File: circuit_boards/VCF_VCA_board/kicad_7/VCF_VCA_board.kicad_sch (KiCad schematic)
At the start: 7 parts, among them J2 MOD_BOARD_CON, J3 VCF_EXT_CON, SW1 SR1712F-0204

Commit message: Progress on circuit boards
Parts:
- added D101, D102: MMSZ5225B-7-F, Diode_SMD:D_SOD-123, symbol Device:D_Zener
- added R103: 1k, Resistor_SMD:R_0603_1608Metric, symbol Device:R
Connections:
- net GND: now also D102.1 (K)
- net VCF: now also R103.1
- new net: D101.2 (A), D102.2 (A)
- new net envelope_VCA/SIGNAL_IN: D101.1 (K), R103.2
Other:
- note removed: "TODO check the pole-mixing scheme, does the dry signal include the feedback or not?"
- moved on the sheet: C101, J2, J3, R101, R102, SW1A

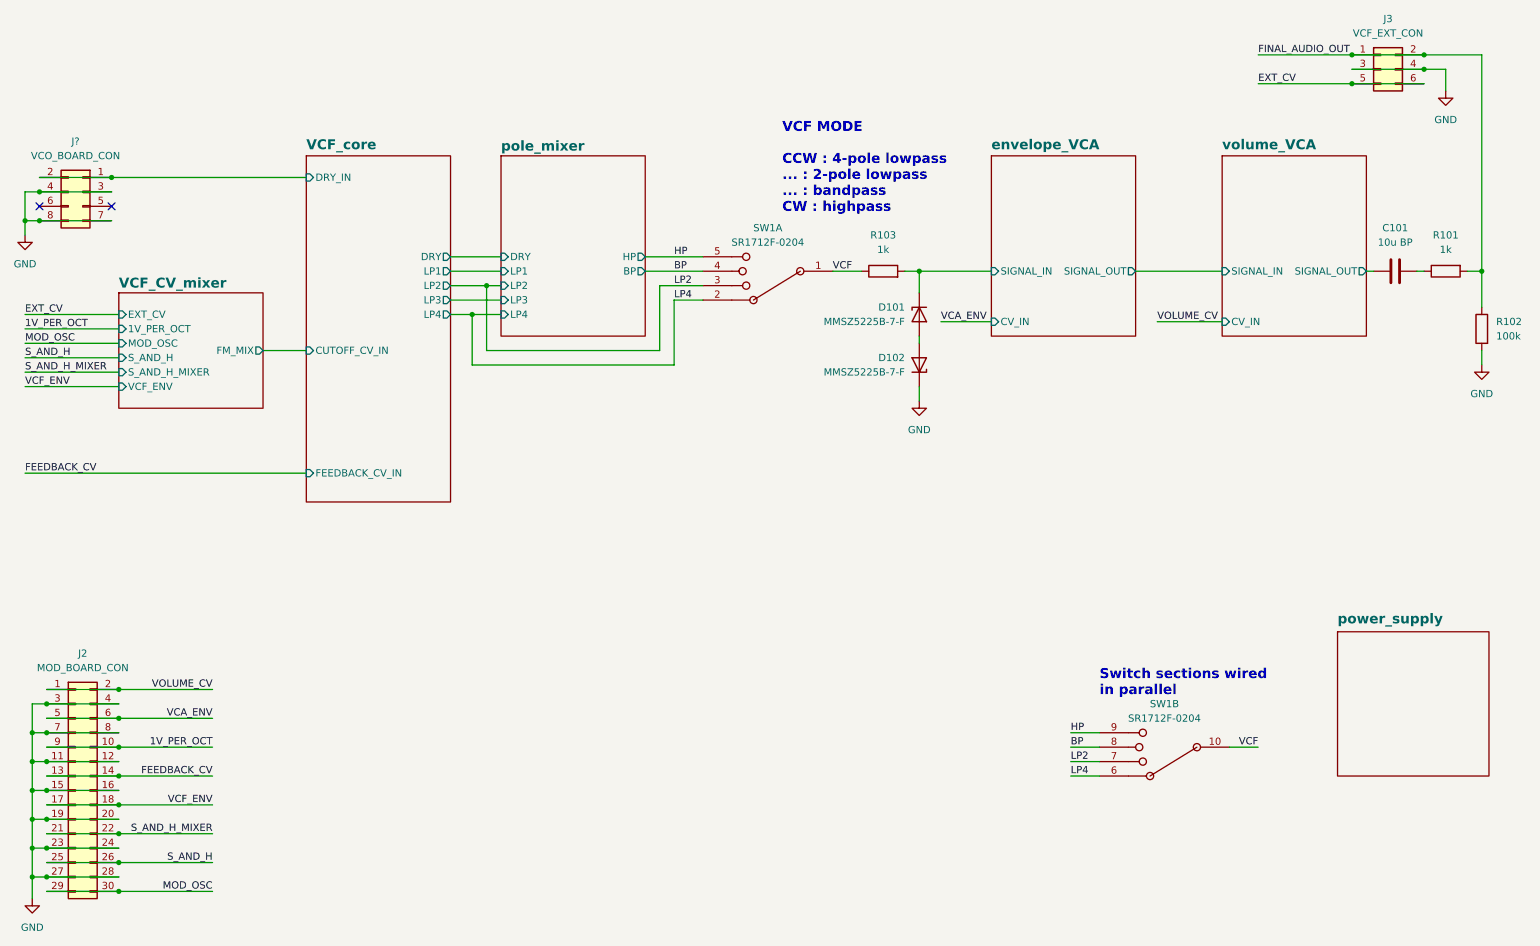
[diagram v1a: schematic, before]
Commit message: Update PCBs, tweak vals, add VCF CV from DAC
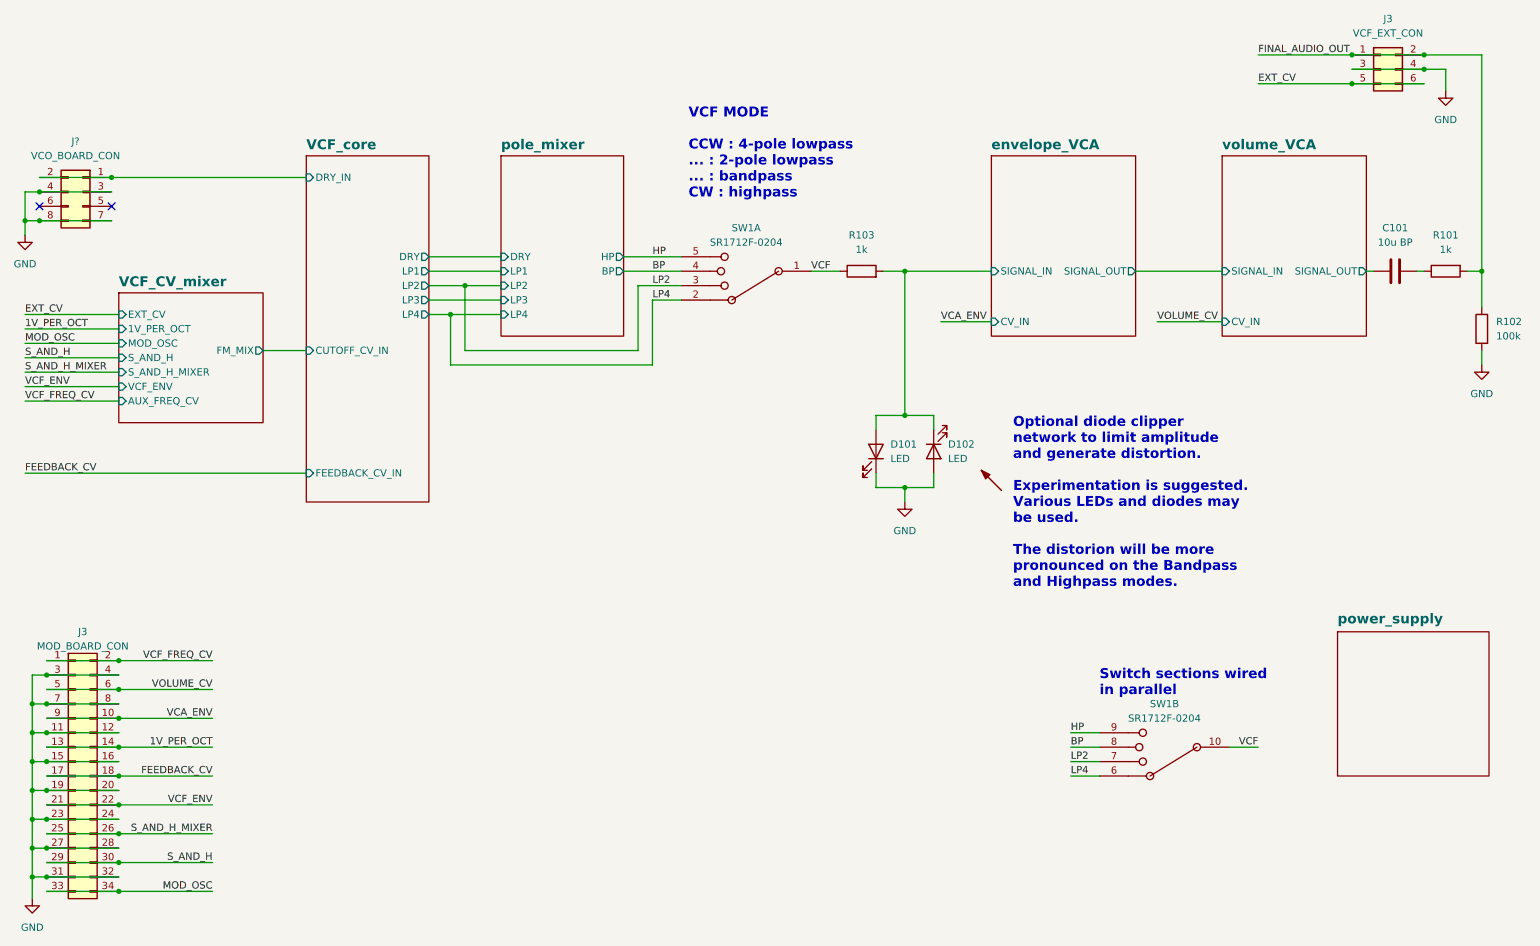
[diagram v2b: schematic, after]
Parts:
- removed D101, D102: MMSZ5225B-7-F, Diode_SMD:D_SOD-123, symbol Device:D_Zener
- removed J2: MOD_BOARD_CON, custom_footprints:30_pin_IDC-Header, symbol Connector_Generic:Conn_02x15_Odd_Even
- added D101, D102: LED, LED_THT:LED_D5.0mm, symbol Device:LED
- added J3: MOD_BOARD_CON, custom_footprints:34_pin_IDC_header, symbol Connector_Generic:Conn_02x17_Odd_Even
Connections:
- net 1V_PER_OCT: now also J3.13 (Pin_13), J3.14 (Pin_14)
- net FEEDBACK_CV: now also J3.17 (Pin_17), J3.18 (Pin_18)
- net GND: now also D101.1 (K), D102.2 (A), J3.11 (Pin_11), J3.12 (Pin_12), J3.15 (Pin_15), J3.16 (Pin_16), J3.19 (Pin_19), J3.20 (Pin_20), J3.23 (Pin_23), J3.24 (Pin_24), J3.27 (Pin_27), J3.28 (Pin_28), J3.3 (Pin_3), J3.31 (Pin_31), J3.32 (Pin_32), J3.4 (Pin_4), J3.7 (Pin_7), J3.8 (Pin_8)
- net MOD_OSC: now also J3.33 (Pin_33), J3.34 (Pin_34)
- net S_AND_H: now also J3.29 (Pin_29), J3.30 (Pin_30)
- net S_AND_H_MIXER: now also J3.25 (Pin_25), J3.26 (Pin_26)
- net VCA_ENV: now also J3.10 (Pin_10), J3.9 (Pin_9)
- net VCF_ENV: now also J3.21 (Pin_21), J3.22 (Pin_22)
- net VOLUME_CV: now also J3.5 (Pin_5), J3.6 (Pin_6)
- net envelope_VCA/SIGNAL_IN: now also D101.2 (A), D102.1 (K)
- new net VCF_FREQ_CV: J3.1 (Pin_1), J3.2 (Pin_2)
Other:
- sheet VCF_CV_mixer ports: added AUX_FREQ_CV; removed none
- note added: "Optional diode clipper network to limit amplitude and generate distortion. Experimentation is suggested. Various LEDs and diodes may be used. The distorion will be more pronounced on the Bandpass and Highpass modes."
- moved on the sheet: R103, SW1A

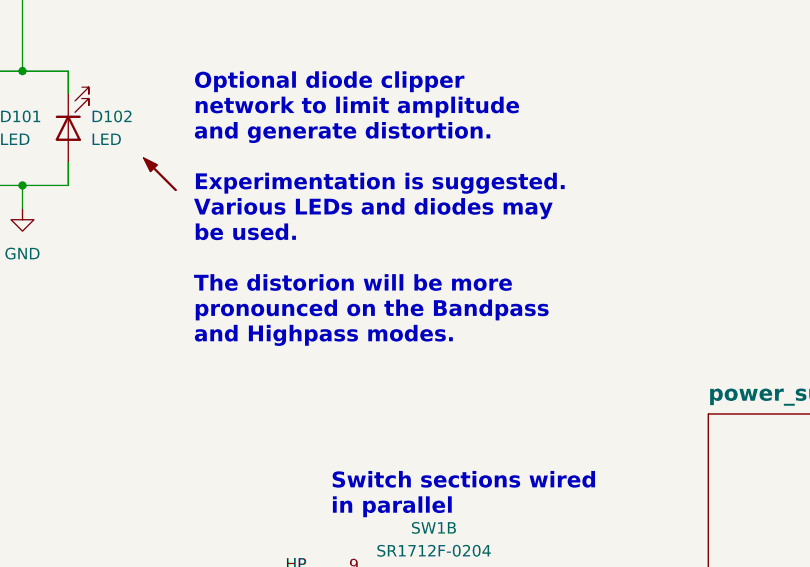
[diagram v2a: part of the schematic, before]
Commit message: Fix typo in note about clipping diodes
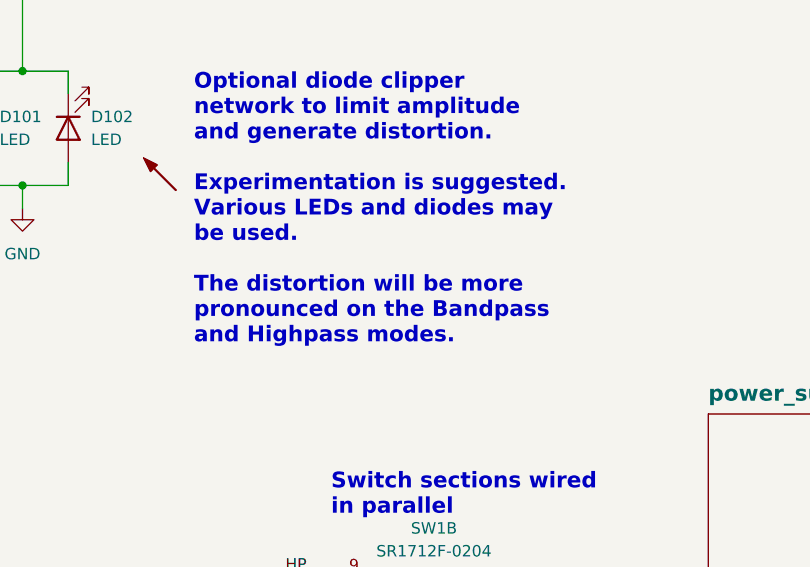
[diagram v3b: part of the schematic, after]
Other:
- note added: "Optional diode clipper network to limit amplitude and generate distortion. Experimentation is suggested. Various LEDs and diodes may be used. The distortion will be more pronounced on the Bandpass and Highpass modes."
- note removed: "Optional diode clipper network to limit amplitude and generate distortion. Experimentation is suggested. Various LEDs and diodes may be used. The distorion will be more pronounced on the Bandpass and Highpass modes."
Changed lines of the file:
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@@
     (stroke (width 0) (type default))
   )
-  (text "Optional diode clipper\nnetwork to limit amplitude\nand generate distortion.\n\nExperimentation is suggested.\nVarious LEDs and diodes may\nbe used.\n\nThe distorion will be more\npronounced on the Bandpass\nand Highpass modes."
+  (text "Optional diode clipper\nnetwork to limit amplitude\nand generate distortion.\n\nExperimentation is suggested.\nVarious LEDs and diodes may\nbe used.\n\nThe distortion will be more\npronounced on the Bandpass\nand Highpass modes."
     (at 194.31 128.27 0)
     (effects (font (size 1.75 1.75) bold) (justify left bottom))
